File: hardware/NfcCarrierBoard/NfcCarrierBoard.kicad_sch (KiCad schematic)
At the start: 56 parts, among them J1 Barrel_Jack, J2 Conn_01x03, J3 JST SH 4, J4 Grove, J5 Conn_01x03, J6 UART, J7 Grove UART, Q1 NMOS, Q2 NMOS, SW1 RESET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

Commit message: Add heatsink pad Add silkscreen
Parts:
- added HS1: TestPoint, TestPoint:TestPoint_Pad_D1.0mm, symbol Connector:TestPoint
- added SYM1: Logo_Open_Hardware_Small, Symbol:OSHW-Logo_19x20mm_SilkScreen, symbol Graphic:Logo_Open_Hardware_Small
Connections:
- new net Heatsink: HS1.1
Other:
- company: EventAccess -> ${COMPANY}
- title: NFC Carrier Board -> ${TITLE}
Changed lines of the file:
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@@
 	(paper "A4")
 	(title_block
-		(title "NFC Carrier Board")
+		(title "${TITLE}")
 		(date "${DATE}")
 		(rev "${REVISION}")
-		(company "EventAccess")
+		(company "${COMPANY}")
 	)
 	(junction
@@
 	)
 	(symbol
+		(lib_id "power:GNDD")
+		(at 156.21 129.54 90)
+		(unit 1)
+		(exclude_from_sim no)
+		(in_bom yes)
+		(on_board yes)
+		(dnp no)
+		(property "Reference" "#PWR053"
+			(at 162.56 129.54 0)
+			(effects
+				(font
+					(size 1.27 1.27)
+				)
+				(hide yes)
+			)
+		)
+		(property "Value" "Heatsink"
+			(at 150.622 132.334 90)
+			(effects
+				(font
+					(size 1.27 1.27)
+				)
+				(justify right)
+			)
+		)
+		(property "Footprint" ""
+			(at 156.21 129.54 0)
+			(effects
+				(font
+					(size 1.27 1.27)
+				)
+				(hide yes)
+			)
+		)
+		(property "Datasheet" ""
+			(at 156.21 129.54 0)
+			(effects
+				(font
+					(size 1.27 1.27)
+				)
+				(hide yes)
+			)
+		)
+		(property "Description" "Power symbol creates a global label with name \"GNDD\" , digital ground"
+			(at 156.21 129.54 0)
+			(effects
+				(font
+					(size 1.27 1.27)
+				)
+				(hide yes)
+			)
+		)
+		(pin "1"
+		)
+		(instances
+			(project ""
+				(path "/766243a7-ad3d-48cd-bfed-d2ecca850827"
+					(reference "#PWR053")
+					(unit 1)
+				)
+			)
+		)
+	)
+	(symbol
 		(lib_id "power:GND")
 		(at 80.01 158.75 0)
@@
 	)
 	(symbol
+		(lib_id "Connector:TestPoint")
+		(at 156.21 129.54 90)
+		(unit 1)
+		(exclude_from_sim no)
+		(in_bom yes)
+		(on_board yes)
+		(dnp no)
+		(property "Reference" "HS1"
+			(at 148.59 129.54 90)
+			(effects
+				(font
+					(size 1.27 1.27)
+				)
+				(hide yes)
+			)
+		)
+		(property "Value" "TestPoint"
+			(at 152.908 127 90)
+			(effects
+				(font
+					(size 1.27 1.27)
+				)
+				(hide yes)
+			)
+		)
+		(property "Footprint" "TestPoint:TestPoint_Pad_D1.0mm"
+			(at 156.21 124.46 0)
+			(effects
+				(font
+					(size 1.27 1.27)
+				)
+				(hide yes)
+			)
+		)
+		(property "Datasheet" "~"
+			(at 156.21 124.46 0)
+			(effects
+				(font
+					(size 1.27 1.27)
+				)
+				(hide yes)
+			)
+		)
+		(property "Description" "test point"
+			(at 156.21 129.54 0)
+			(effects
+				(font
+					(size 1.27 1.27)
+				)
+				(hide yes)
+			)
+		)
+		(pin "1"
+		)
+		(instances
+			(project "NfcCarrierBoard"
+				(path "/766243a7-ad3d-48cd-bfed-d2ecca850827"
+					(reference "HS1")
+					(unit 1)
+				)
+			)
+		)
+	)
+	(symbol
 		(lib_id "Connector_Generic:Conn_01x04")
 		(at 132.08 31.75 0)
@@
 		(dnp no)
 		(fields_autoplaced yes)
-		(property "Reference" "#SYM1"
+		(property "Reference" "SYM1"
 			(at 185.42 92.075 0)
 			(effects
@@
 			)
 		)
-		(property "Footprint" "Symbol:OSHW-Symbol_8.9x8mm_Copper"
+		(property "Footprint" "Symbol:OSHW-Logo_19x20mm_SilkScreen"
 			(at 185.42 99.06 0)
 			(effects
@@
 			(project ""
 				(path "/766243a7-ad3d-48cd-bfed-d2ecca850827"
-					(reference "#SYM1")
+					(reference "SYM1")
 					(unit 1)
 				)

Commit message: Fix rule errors
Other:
- title: ${TITLE} -> ${PROJECT_TITLE}
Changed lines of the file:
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@@
 	(paper "A4")
 	(title_block
-		(title "${TITLE}")
+		(title "${PROJECT_TITLE}")
 		(date "${DATE}")
 		(rev "${REVISION}")
@@
 	)
 	(junction
+		(at 158.75 132.08)
+		(diameter 0)
+		(color 0 0 0 0)
+	)
+	(junction
 		(at 54.61 156.21)
 		(diameter 0)
@@
 	(wire
 		(pts
+			(xy 158.75 130.81) (xy 158.75 132.08)
+		)
+		(stroke
+			(width 0)
+			(type default)
+		)
+	)
+	(wire
+		(pts
 			(xy 162.56 180.34) (xy 160.02 180.34)
 		)
@@
 	(wire
 		(pts
+			(xy 158.75 132.08) (xy 160.02 132.08)
+		)
+		(stroke
+			(width 0)
+			(type default)
+		)
+	)
+	(wire
+		(pts
 			(xy 228.6 73.66) (xy 228.6 69.85)
 		)
@@
 	(wire
 		(pts
+			(xy 157.48 132.08) (xy 158.75 132.08)
+		)
+		(stroke
+			(width 0)
+			(type default)
+		)
+	)
+	(wire
+		(pts
 			(xy 205.74 152.4) (xy 213.36 152.4)
 		)
@@
 	(symbol
 		(lib_id "power:GNDD")
-		(at 156.21 129.54 90)
+		(at 160.02 132.08 90)
 		(unit 1)
 		(exclude_from_sim no)
@@
 		(dnp no)
 		(property "Reference" "#PWR053"
-			(at 162.56 129.54 0)
+			(at 166.37 132.08 0)
 			(effects
 				(font
@@
 		)
 		(property "Value" "Heatsink"
-			(at 150.622 132.334 90)
+			(at 154.432 134.874 90)
 			(effects
 				(font
@@
 		)
 		(property "Footprint" ""
-			(at 156.21 129.54 0)
+			(at 160.02 132.08 0)
 			(effects
 				(font
@@
 		)
 		(property "Datasheet" ""
-			(at 156.21 129.54 0)
+			(at 160.02 132.08 0)
 			(effects
 				(font
@@
 		)
 		(property "Description" "Power symbol creates a global label with name \"GNDD\" , digital ground"
-			(at 156.21 129.54 0)
+			(at 160.02 132.08 0)
 			(effects
 				(font
@@
 	(symbol
 		(lib_id "Connector:TestPoint")
-		(at 156.21 129.54 90)
+		(at 157.48 132.08 90)
 		(unit 1)
 		(exclude_from_sim no)
@@
 		(dnp no)
 		(property "Reference" "HS1"
-			(at 148.59 129.54 90)
+			(at 149.86 132.08 90)
 			(effects
 				(font
@@
 		)
 		(property "Value" "TestPoint"
-			(at 152.908 127 90)
+			(at 154.178 129.54 90)
 			(effects
 				(font
@@
 		)
 		(property "Footprint" "TestPoint:TestPoint_Pad_D1.0mm"
-			(at 156.21 124.46 0)
+			(at 157.48 127 0)
 			(effects
 				(font
@@
 		)
 		(property "Datasheet" "~"
-			(at 156.21 124.46 0)
+			(at 157.48 127 0)
 			(effects
 				(font
@@
 		)
 		(property "Description" "test point"
-			(at 156.21 129.54 0)
+			(at 157.48 132.08 0)
 			(effects
 				(font
@@
 					(unit 1)
 				)
+			)
+		)
+	)
+	(symbol
+		(lib_id "power:PWR_FLAG")
+		(at 158.75 130.81 0)
+		(unit 1)
+		(exclude_from_sim no)
+		(in_bom yes)
+		(on_board yes)
+		(dnp no)
+		(property "Reference" "#FLG04"
+			(at 158.75 128.905 0)
+			(effects
+				(font
+					(size 1.27 1.27)
+				)
+				(hide yes)
+			)
+		)
+		(property "Value" "PWR_FLAG"
+			(at 164.338 133.858 90)
+			(effects
+				(font
+					(size 1.27 1.27)
+				)
+				(justify left)
+			)
+		)
+		(property "Footprint" ""
+			(at 158.75 130.81 0)
+			(effects
+				(font
+					(size 1.27 1.27)
+				)
+				(hide yes)
+			)
+		)
+		(property "Datasheet" "~"
+			(at 158.75 130.81 0)
+			(effects
+				(font
+					(size 1.27 1.27)
+				)
+				(hide yes)
+			)
+		)
+		(property "Description" "Special symbol for telling ERC where power comes from"
+			(at 158.75 130.81 0)
+			(effects
+				(font
+					(size 1.27 1.27)
+				)
+				(hide yes)
+			)
+		)
+		(pin "1"
+		)
+		(instances
+			(project "NfcCarrierBoard"
+				(path "/766243a7-ad3d-48cd-bfed-d2ecca850827"
+					(reference "#FLG04")
+					(unit 1)
+				)

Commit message: Fix off-board silkscreen
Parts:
- SW1: DigiKey (none) -> 2223-TS11-674-105-BK-260-RA-D-ND; DigiKey PN 2223-TS11-674-105-BK-260-RA-D-ND -> (none)
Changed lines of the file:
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@@
 			)
 		)
-		(property "DigiKey PN" "2223-TS11-674-105-BK-260-RA-D-ND"
+		(property "DigiKey" "2223-TS11-674-105-BK-260-RA-D-ND"
 			(at 205.74 139.7 0)
 			(effects

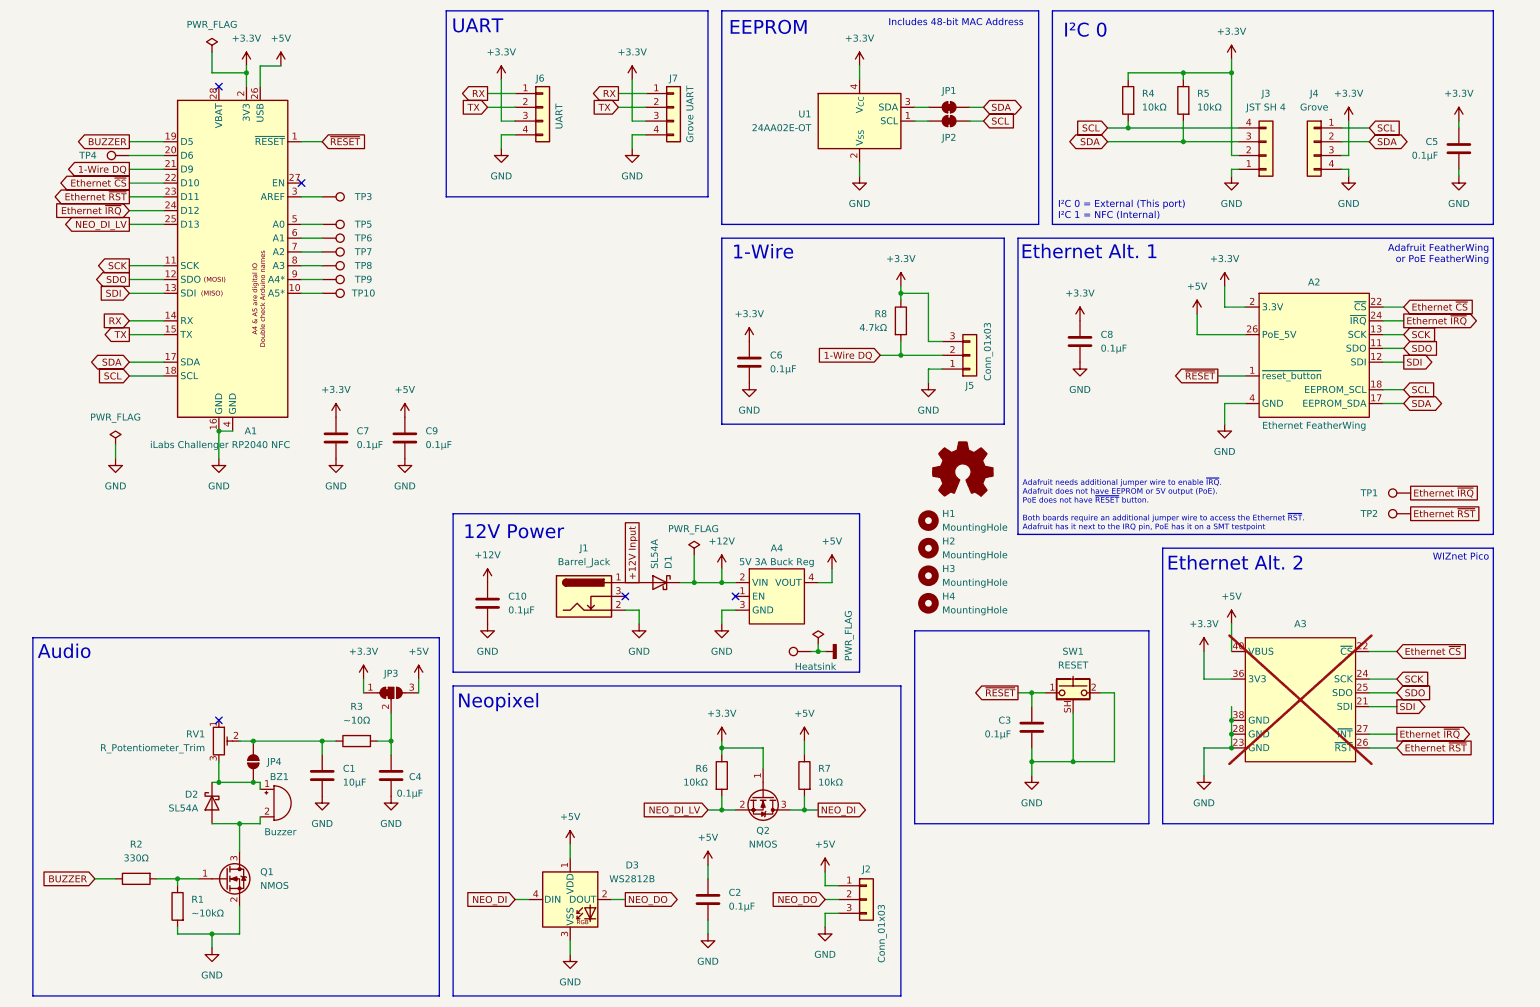
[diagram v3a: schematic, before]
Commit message: Populate part numbers for BOM
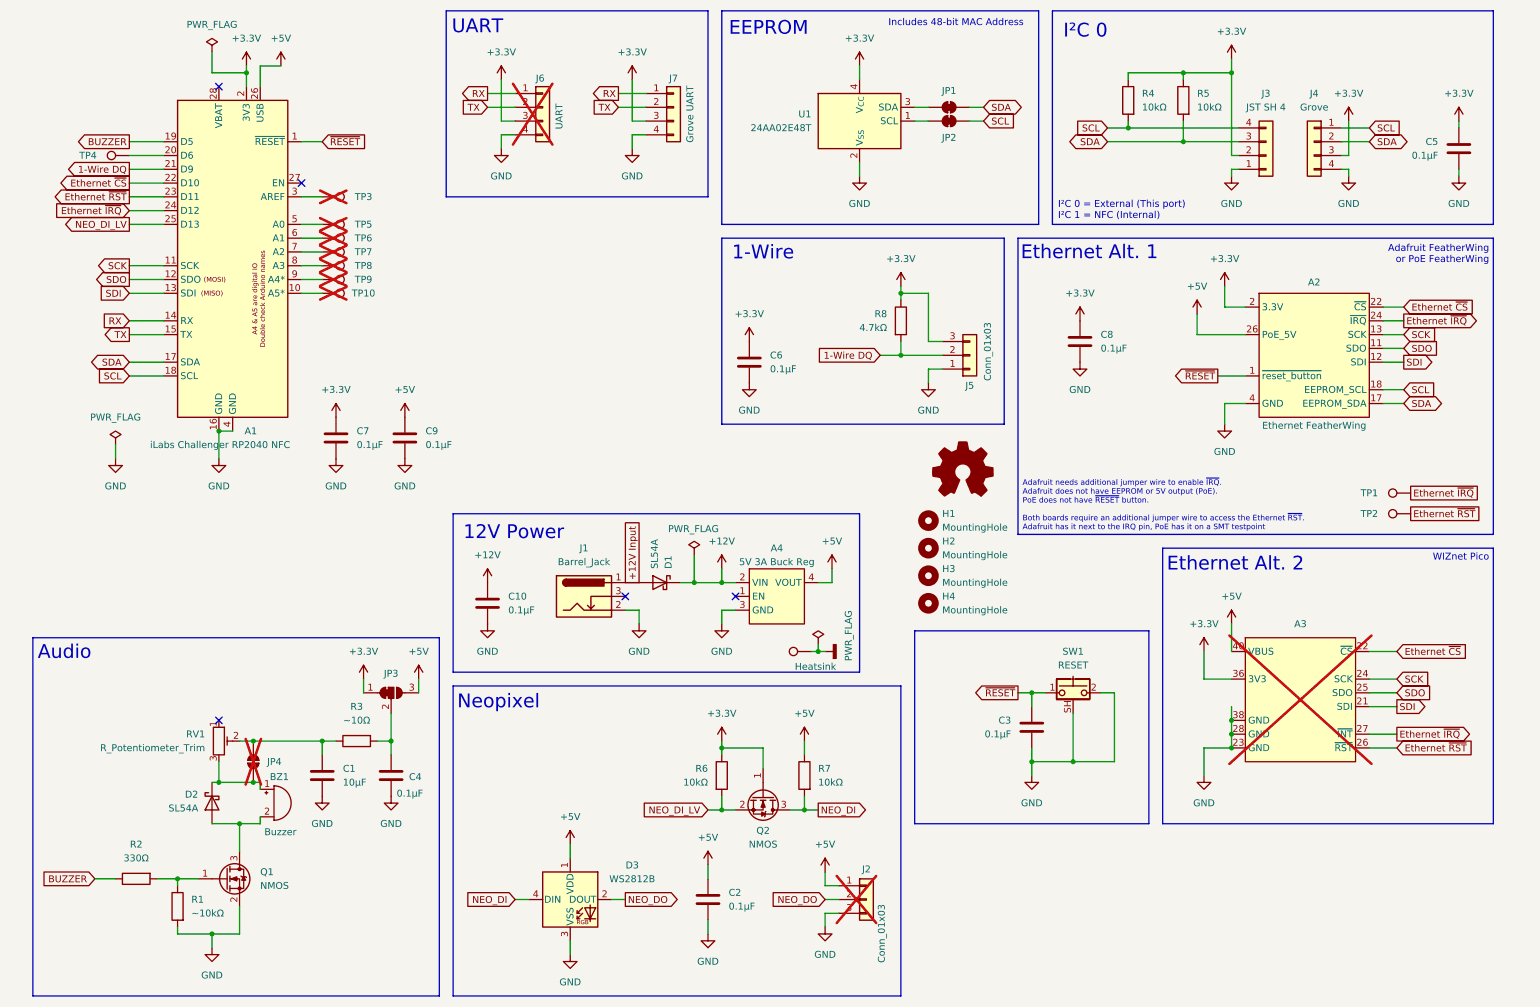
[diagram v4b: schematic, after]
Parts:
- A1: MFN (none) -> iLabs; MPN (none) -> 98-00241-2
- A2: DigiKey (none) -> 1528-1725-ND; MFN (none) -> Adafruit Industries LLC; MPN (none) -> 3201
- A4: MFN (none) -> SparkFun Electronics; MPN (none) -> COM-21256
- BZ1: DigiKey (none) -> 668-1470-ND; MFN (none) -> PUI Audio, Inc.; MPN (none) -> AT-1224-TWT-5V-2-R
- D1, D2: DigiKey (none) -> 1655-SL54ACT-ND; MFN (none) -> SMC Diode Solutions; MPN (none) -> SL54A
- D3: DigiKey (none) -> 1568-COM-16347CT-ND; MFN (none) -> Worldsemi; MPN (none) -> WS2812B
- J1: DigiKey (none) -> CP-002AH-ND; MFN (none) -> Same Sky (Formerly CUI Devices); MPN (none) -> PJ-002AH
- J2, J6, JP4, TP10, TP3, TP5, TP6, TP7, TP8, TP9: now not fitted
- J3: DigiKey (none) -> 455-BM04B-SRSS-TBCT-ND; MFN (none) -> JST Sales America Inc.; MPN (none) -> BM04B-SRSS-TB
- J4, J7: DigiKey (none) -> 1597-1082-ND; MFN (none) -> Seeed Technology Co., Ltd; MPN (none) -> 110990030
- J5: DigiKey (none) -> S7036-ND; MFN (none) -> Sullins Connector Solutions; MPN (none) -> PPPC031LFBN-RC
- Q1, Q2: DigiKey (none) -> BSS138KCT-ND; MFN (none) -> onsemi; MPN (none) -> BSS138K
- U1: value 24AA02E-OT -> 24AA02E48T; DigiKey (none) -> 24AA02E48T-I/OTCT-ND; MFN (none) -> Microchip Technology; MPN (none) -> 24AA02E48T-I/OT

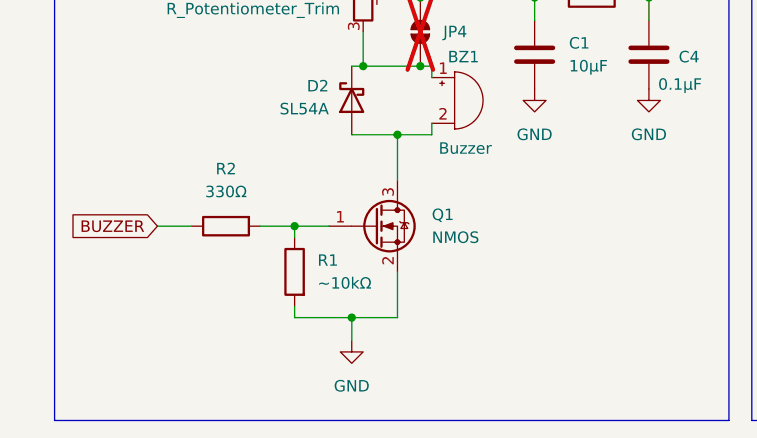
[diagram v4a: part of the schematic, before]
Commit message: Populate resistors for BOM
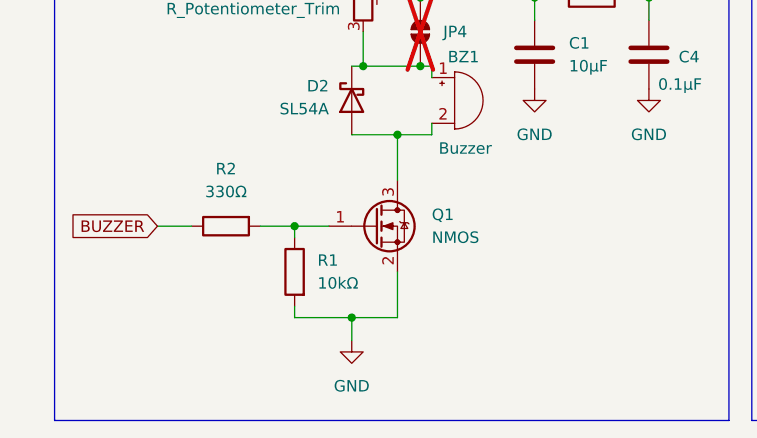
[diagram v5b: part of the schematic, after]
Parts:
- A1, RV1, SYM1: DigiKey (none) -> -
- H1, H2, H3, H4, HS1, TP1, TP10, TP2, TP3, TP4, TP5, TP6, TP7, TP8, TP9: DigiKey (none) -> -; MPN (none) -> -
- R1: value ~10kΩ -> 10kΩ; DigiKey (none) -> RMCF0805FT10K0CT-ND; MFN (none) -> Stackpole Electronics Inc; MPN (none) -> RMCF0805FT10K0
- R2: DigiKey (none) -> RMCF0805FT330RCT-ND; MFN (none) -> Stackpole Electronics Inc; MPN (none) -> RMCF0805FT330R
- R3: DigiKey (none) -> 541-10.0TCT-ND; MFN (none) -> Vishay Dale; MPN (none) -> CRCW080510R0FKEAHP
- R4, R5, R6, R7: DigiKey (none) -> RMCF0805FT10K0CT-ND; MFN (none) -> Stackpole Electronics Inc; MPN (none) -> RMCF0805FT10K0
- R8: DigiKey (none) -> RMCF0805FT4K70CT-ND; MFN (none) -> Stackpole Electronics Inc; MPN (none) -> RMCF0805FT4K70

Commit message: Populate capacitors for BOM
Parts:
- C1: DigiKey (none) -> 1276-3100-1-ND; MFN (none) -> Samsung Electro-Mechanics; MPN (none) -> CL31B106KAHNFNE
- C10, C2, C3, C4, C5, C6, C7, C8, C9: DigiKey (none) -> 1276-1942-1-ND; MFN (none) -> Samsung Electro-Mechanics; MPN (none) -> CL10B105KA8NFNC
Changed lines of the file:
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@@
 			)
 		)
-		(property "Description" "Unpolarized capacitor"
+		(property "Description" "Decopuling; note! DC bias voltage derating"
 			(at 97.79 123.19 0)
 			(effects
@@
 			)
 		)
-		(property "MFN" ""
+		(property "MFN" "Samsung Electro-Mechanics"
+			(at 97.79 123.19 0)
+			(effects
+				(font
+					(size 1.27 1.27)
+				)
+				(hide yes)
+			)
+		)
+		(property "DigiKey" "1276-1942-1-ND"
+			(at 97.79 123.19 0)
+			(effects
+				(font
+					(size 1.27 1.27)
+				)
+				(hide yes)
+			)
+		)
+		(property "MPN" "CL10B105KA8NFNC"
 			(at 97.79 123.19 0)
 			(effects
@@
 			)
 		)
-		(property "Description" "Unpolarized capacitor"
+		(property "Description" "Decopuling; note! DC bias voltage derating"
 			(at 207.01 74.93 0)
 			(effects
@@
 			)
 		)
-		(property "MFN" ""
+		(property "MFN" "Samsung Electro-Mechanics"
+			(at 207.01 74.93 0)
+			(effects
+				(font
+					(size 1.27 1.27)
+				)
+				(hide yes)
+			)
+		)
+		(property "DigiKey" "1276-1942-1-ND"
+			(at 207.01 74.93 0)
+			(effects
+				(font
+					(size 1.27 1.27)
+				)
+				(hide yes)
+			)
+		)
+		(property "MPN" "CL10B105KA8NFNC"
 			(at 207.01 74.93 0)
 			(effects
@@
 			)
 		)
-		(property "Description" "Unpolarized capacitor"
+		(property "Description" "Decopuling"
 			(at 67.31 154.94 0)
 			(effects
@@
 			)
 		)
-		(property "MFN" ""
+		(property "MFN" "Samsung Electro-Mechanics"
+			(at 67.31 154.94 0)
+			(effects
+				(font
+					(size 1.27 1.27)
+				)
+				(hide yes)
+			)
+		)
+		(property "DigiKey" "1276-3100-1-ND"
+			(at 67.31 154.94 0)
+			(effects
+				(font
+					(size 1.27 1.27)
+				)
+				(hide yes)
+			)
+		)
+		(property "MPN" "CL31B106KAHNFNE"
 			(at 67.31 154.94 0)
 			(effects
@@
 			)
 		)
-		(property "Description" "Unpolarized capacitor"
+		(property "Description" "Decopuling; note! DC bias voltage derating"
 			(at 138.43 177.8 0)
 			(effects
@@
 			)
 		)
-		(property "MFN" ""
+		(property "MFN" "Samsung Electro-Mechanics"
+			(at 138.43 177.8 0)
+			(effects
+				(font
+					(size 1.27 1.27)
+				)
+				(hide yes)
+			)
+		)
+		(property "DigiKey" "1276-1942-1-ND"
+			(at 138.43 177.8 0)
+			(effects
+				(font
+					(size 1.27 1.27)
+				)
+				(hide yes)
+			)
+		)
+		(property "MPN" "CL10B105KA8NFNC"
 			(at 138.43 177.8 0)
 			(effects
@@
 			)
 		)
-		(property "Description" "Unpolarized capacitor"
+		(property "Description" "Decopuling; note! DC bias voltage derating"
 			(at 276.86 39.37 0)
 			(effects
@@
 			)
 		)
-		(property "MFN" ""
+		(property "MFN" "Samsung Electro-Mechanics"
+			(at 276.86 39.37 0)
+			(effects
+				(font
+					(size 1.27 1.27)
+				)
+				(hide yes)
+			)
+		)
+		(property "DigiKey" "1276-1942-1-ND"
+			(at 276.86 39.37 0)
+			(effects
+				(font
+					(size 1.27 1.27)
+				)
+				(hide yes)
+			)
+		)
+		(property "MPN" "CL10B105KA8NFNC"
 			(at 276.86 39.37 0)
 			(effects
@@
 			)
 		)
-		(property "Description" "Unpolarized capacitor"
+		(property "Description" "Decopuling; note! DC bias voltage derating"
 			(at 69.85 92.71 0)
 			(effects
@@
 			)
 		)
-		(property "MFN" ""
+		(property "MFN" "Samsung Electro-Mechanics"
+			(at 69.85 92.71 0)
+			(effects
+				(font
+					(size 1.27 1.27)
+				)
+				(hide yes)
+			)
+		)
+		(property "DigiKey" "1276-1942-1-ND"
+			(at 69.85 92.71 0)
+			(effects
+				(font
+					(size 1.27 1.27)
+				)
+				(hide yes)
+			)
+		)
+		(property "MPN" "CL10B105KA8NFNC"
 			(at 69.85 92.71 0)
 			(effects
@@
 			)
 		)
-		(property "Description" "Unpolarized capacitor"
+		(property "Description" "Decopuling; note! DC bias voltage derating"
 			(at 146.05 78.74 0)
 			(effects
@@
 			)
 		)
-		(property "MFN" ""
+		(property "MFN" "Samsung Electro-Mechanics"
+			(at 146.05 78.74 0)
+			(effects
+				(font
+					(size 1.27 1.27)
+				)
+				(hide yes)
+			)
+		)
+		(property "DigiKey" "1276-1942-1-ND"
+			(at 146.05 78.74 0)
+			(effects
+				(font
+					(size 1.27 1.27)
+				)
+				(hide yes)
+			)
+		)
+		(property "MPN" "CL10B105KA8NFNC"
 			(at 146.05 78.74 0)
 			(effects
@@
 			)
 		)
-		(property "Description" "Unpolarized capacitor"
+		(property "Description" "Decopuling; note! DC bias voltage derating"
 			(at 82.55 92.71 0)
 			(effects
@@
 			)
 		)
-		(property "MFN" ""
+		(property "MFN" "Samsung Electro-Mechanics"
+			(at 82.55 92.71 0)
+			(effects
+				(font
+					(size 1.27 1.27)
+				)
+				(hide yes)
+			)
+		)
+		(property "DigiKey" "1276-1942-1-ND"
+			(at 82.55 92.71 0)
+			(effects
+				(font
+					(size 1.27 1.27)
+				)
+				(hide yes)
+			)
+		)
+		(property "MPN" "CL10B105KA8NFNC"
 			(at 82.55 92.71 0)
 			(effects
@@
 			)
 		)
-		(property "Description" "Unpolarized capacitor"
+		(property "Description" "Decopuling; note! DC bias voltage derating"
 			(at 198.12 146.05 0)
 			(effects
@@
 			)
 		)
-		(property "MFN" ""
+		(property "MFN" "Samsung Electro-Mechanics"
+			(at 198.12 146.05 0)
+			(effects
+				(font
+					(size 1.27 1.27)
+				)
+				(hide yes)
+			)
+		)
+		(property "DigiKey" "1276-1942-1-ND"
+			(at 198.12 146.05 0)
+			(effects
+				(font
+					(size 1.27 1.27)
+				)
+				(hide yes)
+			)
+		)
+		(property "MPN" "CL10B105KA8NFNC"
 			(at 198.12 146.05 0)
 			(effects
@@
 			)
 		)
-		(property "Description" "Unpolarized capacitor"
+		(property "Description" "Decopuling; note! DC bias voltage derating"
 			(at 80.01 154.94 0)
 			(effects
@@
 			)
 		)
-		(property "MFN" ""
+		(property "MFN" "Samsung Electro-Mechanics"
+			(at 80.01 154.94 0)
+			(effects
+				(font
+					(size 1.27 1.27)
+				)
+				(hide yes)
+			)
+		)
+		(property "DigiKey" "1276-1942-1-ND"
+			(at 80.01 154.94 0)
+			(effects
+				(font
+					(size 1.27 1.27)
+				)
+				(hide yes)
+			)
+		)
+		(property "MPN" "CL10B105KA8NFNC"
 			(at 80.01 154.94 0)
 			(effects
